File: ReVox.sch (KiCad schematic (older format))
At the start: 42 parts, among them CN1 EXPANSION_PORT, CN2 RAW_OUT, CN3 AMP_OUT, CN4 CN_RAW_DAC, U1 GAL20V8, U2 74LS273, U3 TLC272

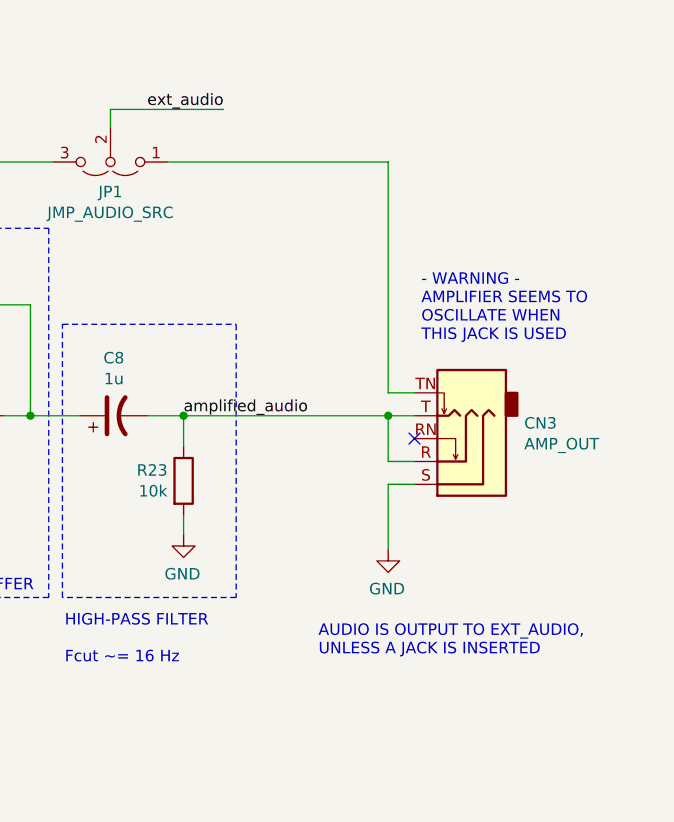
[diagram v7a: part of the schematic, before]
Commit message: Remove amplified output jack This makes the opamp oscillate and is totally unnecessary
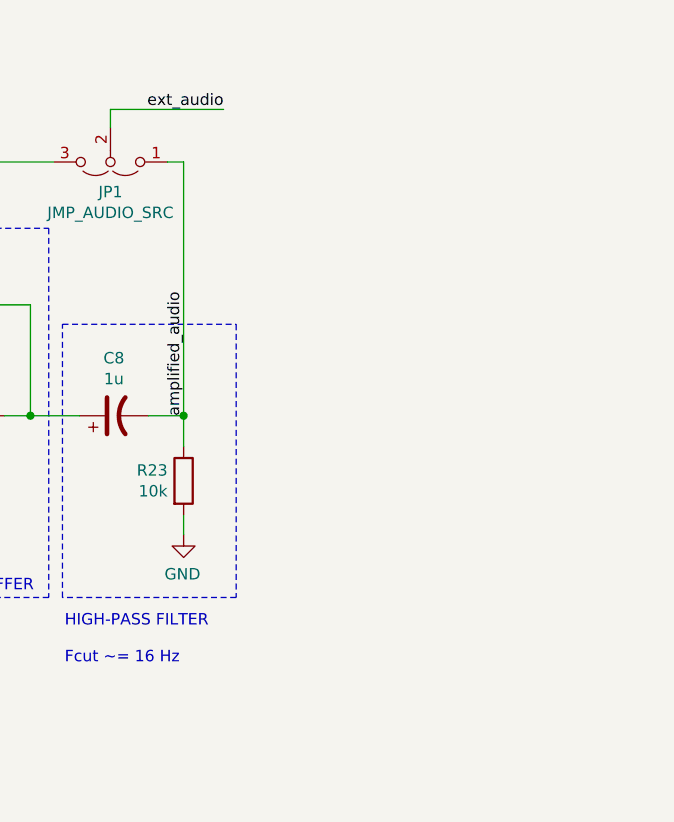
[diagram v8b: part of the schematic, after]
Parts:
- removed CN3: AMP_OUT, ReVox:AudioJack_SJ1-3525N, symbol Connector:AudioJack3_SwitchTR
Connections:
- net amplified_audio: now also JP1.1 (A)
- no-connect marks 17 -> 16
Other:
- note removed: "- WARNING -\nAMPLIFIER SEEMS TO\nOSCILLATE WHEN\nTHIS JACK IS USED"
- note removed: "AUDIO IS OUTPUT TO EXT_AUDIO,\nUNLESS A JACK IS INSERTED"
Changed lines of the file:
@@
 Sheet 1 1
 Title "ReVox"
-Date "2023-10-29"
+Date "2023-11-17"
 Rev "1git"
 Comp "SukkoPera"
@@
 Text Label 13920 4860 2    50   ~ 0
 ext_audio
-Text Label 13745 6200 0    50   ~ 0
+Text Label 13745 6200 1    50   ~ 0
 amplified_audio
 Wire Wire Line
-	14640 6500 14640 6785
-Wire Wire Line
-	14640 6400 14640 6200
-$Comp
-L power:GND #PWR?
-U 1 1 65C5C679
-P 14640 6785
-AR Path="/6579482E/65C5C679" Ref="#PWR?"  Part="1"
-AR Path="/65C5C679" Ref="#PWR0102"  Part="1"
-AR Path="/65BF4077/65C5C679" Ref="#PWR?"  Part="1"
-F 0 "#PWR0102" H 14640 6535 50  0001 C CNN
-F 1 "GND" H 14645 6612 50  0000 C CNN
-F 2 "" H 14640 6785 50  0001 C CNN
-F 3 "" H 14640 6785 50  0001 C CNN
-	1    14640 6785
-	-1   0    0    -1
-$EndComp
-Wire Wire Line
-	14755 6500 14640 6500
-Wire Wire Line
-	14755 6400 14640 6400
-Connection ~ 14640 6200
-Wire Wire Line
-	14640 6200 14755 6200
-NoConn ~ 14755 6300
-Wire Wire Line
-	14755 6100 14640 6100
-Text Notes 14335 7255 0    50   ~ 0
-AUDIO IS OUTPUT TO EXT_AUDIO,\nUNLESS A JACK IS INSERTED
-Wire Wire Line
-	13675 5090 14640 5090
-Wire Wire Line
-	14640 5090 14640 6100
+	13675 5090 13745 5090
 $Comp
 L Amplifier_Operational:TLC272 U3
@@
 Wire Wire Line
 	10045 6000 10155 6000
-$Comp
-L Connector:AudioJack3_SwitchTR CN?
-U 1 1 65C5C687
-P 14955 6400
-AR Path="/6579482E/65C5C687" Ref="CN?"  Part="1"
-AR Path="/65C5C687" Ref="CN3"  Part="1"
-AR Path="/65BF4077/65C5C687" Ref="CN?"  Part="1"
-F 0 "CN3" H 14675 6233 50  0000 R CNN
-F 1 "AMP_OUT" H 14675 6324 50  0000 R CNN
-F 2 "ReVox:AudioJack_SJ1-3525N" H 14955 6400 50  0001 C CNN
-F 3 "~" H 14955 6400 50  0001 C CNN
-F 4 "490-SJ1-3525N" H 14955 6400 50  0001 C CNN "MouserPN"
-F 5 "AUDIO_OUT" H 14955 6400 50  0001 C CNN "Value"
-	1    14955 6400
-	-1   0    0    1
-$EndComp
 Wire Wire Line
 	8080 6385 8080 6000
@@
 	1    0    0    -1
 $EndComp
-Wire Wire Line
-	13745 6200 14640 6200
 Connection ~ 13745 6200
 Text Notes 6095 8085 2    50   ~ 0
@@
 Text Notes 13225 7290 0    50   ~ 0
 HIGH-PASS FILTER\n\nFcut ~~= 16 Hz
-Text Notes 14785 5880 0    50   ~ 0
-- WARNING -\nAMPLIFIER SEEMS TO\nOSCILLATE WHEN\nTHIS JACK IS USED
 Text Notes 5125 10120 0    50   ~ 0
 This is the bias voltage for the opamp.\nIt is set at +2V because the TLC272\nswings between 0 and 4V. If using a\nrail-to-rail opamp (like the LMC6482,\nfor instance), this can be set at 2.5V\nby using the same value for R17 and\nR18 (hint: 11k works fine if already\nused for the resistor ladder).
+Wire Wire Line
+	13745 6200 13745 5090
 Wire Bus Line
 	11565 1885 11565 3425
